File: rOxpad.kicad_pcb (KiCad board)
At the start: 2 copper layers, 68.3 x 65.1 mm, 25 parts, among them SW1 SW_Push, U1 ATmega16U2-A, U2 PRTR5V0U2X, Y1 16MHz

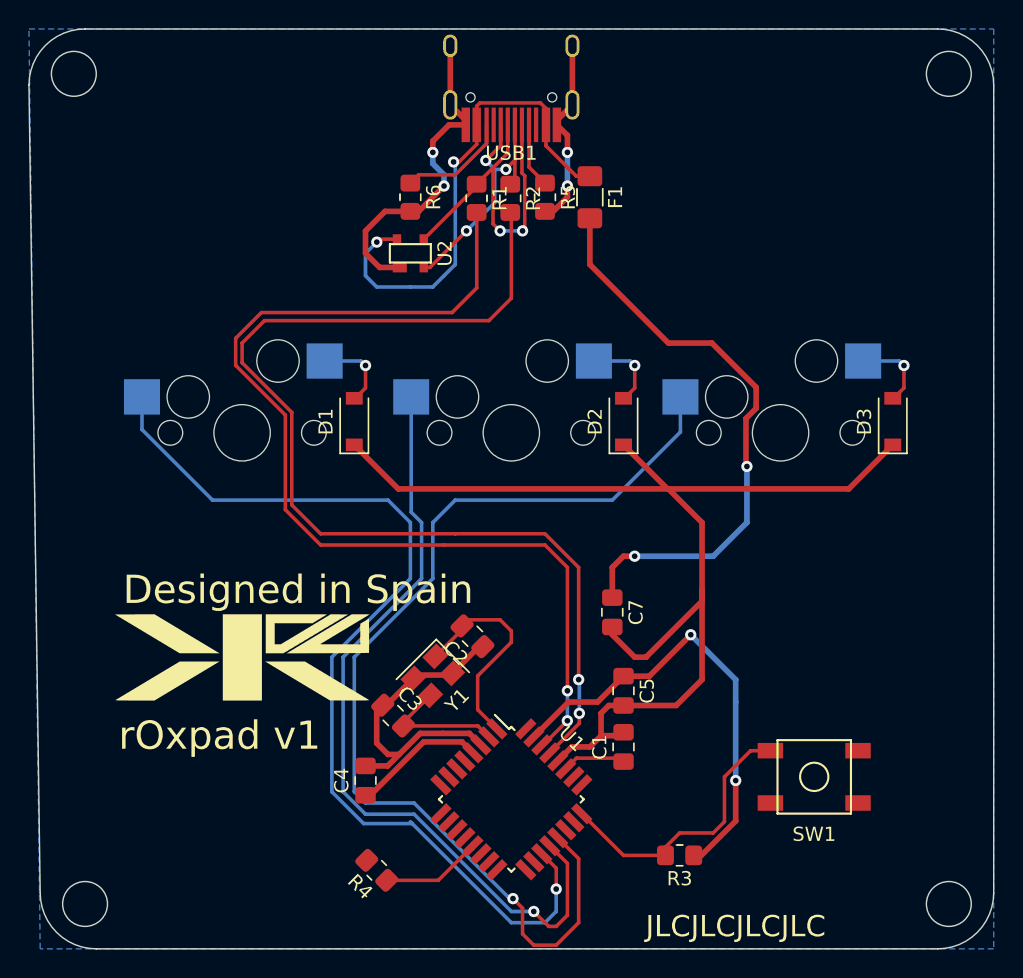
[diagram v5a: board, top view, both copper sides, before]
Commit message: it was a square oops
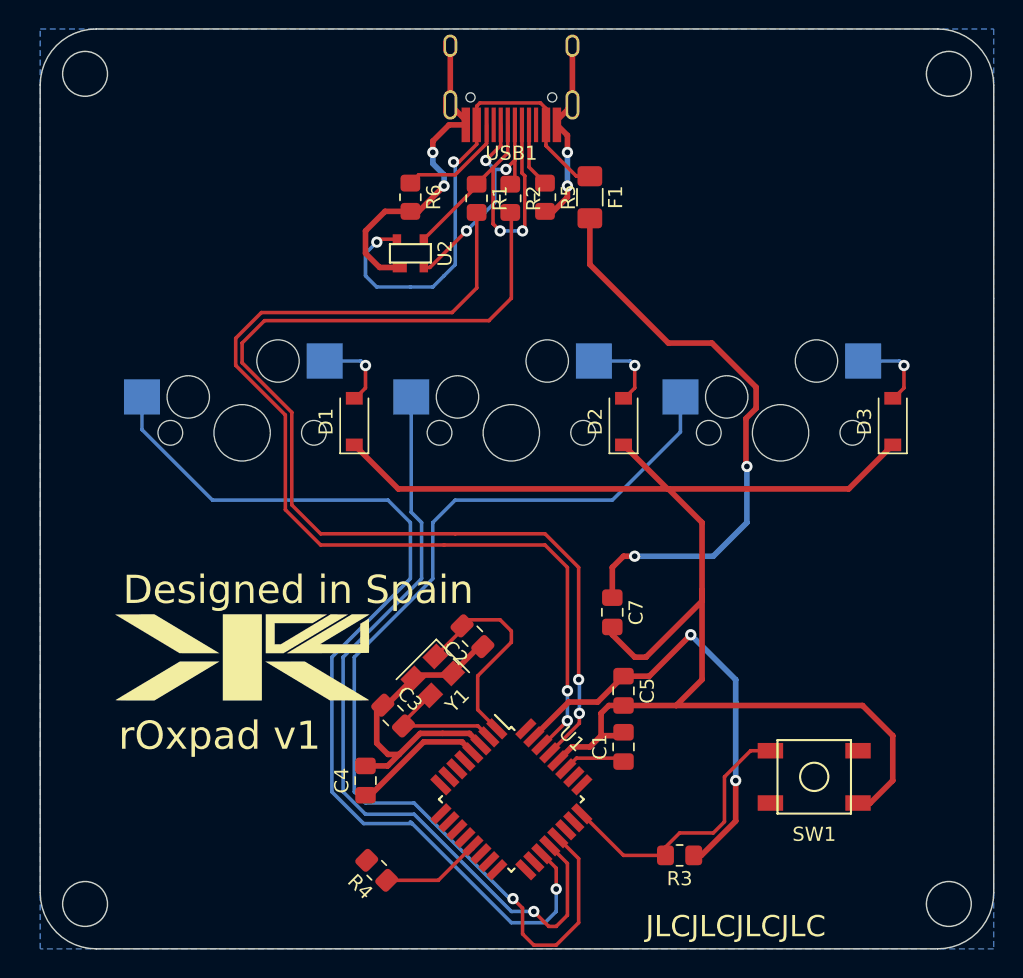
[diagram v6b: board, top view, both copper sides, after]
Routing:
- net GND: track 145.0 -> 167.5 mm
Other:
- board size 68.3 x 65.1 mm -> 67.5 x 65.1 mm
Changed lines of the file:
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@@
   (gr_line (start 77.7875 125.4125) (end 137.31875 125.4125) (layer "Edge.Cuts") (width 0.1))
   (gr_arc (start 137.31875 60.325) (mid 140.12508 61.48742) (end 141.2875 64.29375) (layer "Edge.Cuts") (width 0.1))
-  (gr_circle (center 76.2 63.5) (end 76.2 61.9125) (layer "Edge.Cuts") (width 0.1) (fill none))
-  (gr_line (start 137.31875 60.325) (end 76.99375 60.325) (layer "Edge.Cuts") (width 0.1))
+  (gr_circle (center 76.99375 63.5) (end 76.99375 61.9125) (layer "Edge.Cuts") (width 0.1) (fill none))
+  (gr_line (start 137.31875 60.325) (end 77.7875 60.325) (layer "Edge.Cuts") (width 0.1))
   (gr_line (start 141.2875 121.44375) (end 141.2875 79.375) (layer "Edge.Cuts") (width 0.1))
-  (gr_line (start 73.025 64.29375) (end 73.81875 121.44375) (layer "Edge.Cuts") (width 0.1))
+  (gr_line (start 73.81875 64.29375) (end 73.81875 121.44375) (layer "Edge.Cuts") (width 0.1))
   (gr_circle (center 76.99375 122.2375) (end 76.99375 120.65) (layer "Edge.Cuts") (width 0.1) (fill none))
   (gr_line (start 141.2875 79.375) (end 141.2875 64.29375) (layer "Edge.Cuts") (width 0.1))
-  (gr_arc (start 73.025 64.29375) (mid 74.18742 61.48742) (end 76.99375 60.325) (layer "Edge.Cuts") (width 0.1))
+  (gr_arc (start 73.81875 64.29375) (mid 74.98117 61.48742) (end 77.7875 60.325) (layer "Edge.Cuts") (width 0.1))
   (gr_text "Designed in Spain" (at 92.075 100.0125) (layer "F.SilkS")
     (effects (font (size 2 2) (thickness 0.15)))
@@
   (gr_text "JLCJLCJLCJLC" (at 123.03125 123.825) (layer "F.SilkS")
     (effects (font (size 1.5 1.5) (thickness 0.3)))
-  )
-  (dimension (type aligned) (layer "B.CrtYd")
-    (pts (xy 78.58125 79.375) (xy 73.025 79.375))
-    (height 0)
-    (gr_text "5.5563 mm" (at 75.803125 78.225) (layer "B.CrtYd")
-      (effects (font (size 1 1) (thickness 0.15)))
-    )
-    (format (units 3) (units_format 1) (precision 4))
-    (style (thickness 0.05) (arrow_length 1.27) (text_position_mode 0) (extension_height 0.58642) (extension_offset 0.5) keep_text_aligned)
-  )
-  (dimension (type aligned) (layer "B.CrtYd")
-    (pts (xy 135.73125 79.375) (xy 141.2875 79.375))
-    (height 0)
-    (gr_text "5.5563 mm" (at 138.509375 78.225) (layer "B.CrtYd")
-      (effects (font (size 1 1) (thickness 0.15)))
-    )
-    (format (units 3) (units_format 1) (precision 4))
-    (style (thickness 0.05) (arrow_length 1.27) (text_position_mode 0) (extension_height 0.58642) (extension_offset 0.5) keep_text_aligned)
   )
   (segment (start 103.657639 110.766953) (end 104.433889 111.543203) (width 0.4) (layer "F.Cu") (net 1))
@@
   (segment (start 114.05625 108.19375) (end 115.09375 108.19375) (width 0.4) (layer "F.Cu") (net 2))
   (segment (start 100.6 73.23125) (end 102.39375 71.4375) (width 0.4) (layer "F.Cu") (net 2))
+  (segment (start 132.55625 115.09375) (end 134.14375 113.50625) (width 0.4) (layer "F.Cu") (net 2))
   (segment (start 118.26875 92.86875) (end 131.03125 92.86875) (width 0.4) (layer "F.Cu") (net 2))
   (segment (start 96.8375 74.6125) (end 98.21875 73.23125) (width 0.4) (layer "F.Cu") (net 2))
@@
   (segment (start 97.63125 110.8625) (end 97.63125 108.601504) (width 0.4) (layer "F.Cu") (net 2))
   (segment (start 111.428186 111.125) (end 112.7125 111.125) (width 0.4) (layer "F.Cu") (net 2))
+  (segment (start 134.14375 113.50625) (end 134.14375 110.33125) (width 0.4) (layer "F.Cu") (net 2))
   (segment (start 105.139953 104.027293) (end 104.874788 104.027293) (width 0.4) (layer "F.Cu") (net 2))
   (segment (start 109.5375 73.23125) (end 110.125 73.23125) (width 0.4) (layer "F.Cu") (net 2))
@@
   (segment (start 102.8617 106.040381) (end 102.978858 105.923223) (width 0.4) (layer "F.Cu") (net 2))
   (segment (start 98.425 111.65625) (end 97.63125 110.8625) (width 0.4) (layer "F.Cu") (net 2))
+  (segment (start 134.14375 110.33125) (end 132.00625 108.19375) (width 0.4) (layer "F.Cu") (net 2))
   (segment (start 97.8375 77.2) (end 96.8375 76.2) (width 0.4) (layer "F.Cu") (net 2))
   (segment (start 111.125 67.85375) (end 110.38125 67.11) (width 0.4) (layer "F.Cu") (net 2))
@@
   (segment (start 120.65 100.80625) (end 120.65 100.0125) (width 0.4) (layer "F.Cu") (net 2))
   (segment (start 98.060047 108.172707) (end 98.325212 108.172707) (width 0.4) (layer "F.Cu") (net 2))
+  (segment (start 131.6875 115.09375) (end 132.55625 115.09375) (width 0.4) (layer "F.Cu") (net 2))
   (segment (start 103.93125 66.79) (end 102.83625 65.695) (width 0.4) (layer "F.Cu") (net 2))
   (segment (start 114.3 102.6375) (end 114.3 103.1875) (width 0.4) (layer "F.Cu") (net 2))
@@
   (segment (start 96.04375 89.75625) (end 99.15625 92.86875) (width 0.4) (layer "F.Cu") (net 2))
   (segment (start 96.8375 76.2) (end 96.8375 74.6125) (width 0.4) (layer "F.Cu") (net 2))
+  (segment (start 132.00625 108.19375) (end 118.81875 108.19375) (width 0.4) (layer "F.Cu") (net 2))
   (segment (start 104.999574 110.977518) (end 104.189009 110.166953) (width 0.4) (layer "F.Cu") (net 2))
   (segment (start 99.21875 111.65625) (end 98.425 111.65625) (width 0.4) (layer "F.Cu") (net 2))
@@
         (xy 141.2875 125.4125)
         (xy 73.81875 125.4125)
-        (xy 73.025 60.325)
+        (xy 73.81875 60.325)
         (xy 141.2875 60.325)
       )

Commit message: Fix sizing
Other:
- board size 67.5 x 65.1 mm -> 68.3 x 65.1 mm
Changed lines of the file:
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@@
   (gr_arc (start 141.2875 121.44375) (mid 140.12508 124.25008) (end 137.31875 125.4125) (layer "Edge.Cuts") (width 0.1))
   (gr_circle (center 138.1125 122.2375) (end 139.7 122.2375) (layer "Edge.Cuts") (width 0.1) (fill none))
-  (gr_arc (start 77.7875 125.4125) (mid 74.98117 124.25008) (end 73.81875 121.44375) (layer "Edge.Cuts") (width 0.1))
-  (gr_line (start 77.7875 125.4125) (end 137.31875 125.4125) (layer "Edge.Cuts") (width 0.1))
+  (gr_arc (start 76.99375 125.4125) (mid 74.187402 124.250083) (end 73.025 121.44375) (layer "Edge.Cuts") (width 0.1))
+  (gr_line (start 76.99375 125.4125) (end 137.31875 125.4125) (layer "Edge.Cuts") (width 0.1))
   (gr_arc (start 137.31875 60.325) (mid 140.12508 61.48742) (end 141.2875 64.29375) (layer "Edge.Cuts") (width 0.1))
-  (gr_circle (center 76.99375 63.5) (end 76.99375 61.9125) (layer "Edge.Cuts") (width 0.1) (fill none))
-  (gr_line (start 137.31875 60.325) (end 77.7875 60.325) (layer "Edge.Cuts") (width 0.1))
+  (gr_circle (center 76.2 63.5) (end 76.2 61.9125) (layer "Edge.Cuts") (width 0.1) (fill none))
+  (gr_line (start 137.31875 60.325) (end 76.99375 60.325) (layer "Edge.Cuts") (width 0.1))
   (gr_line (start 141.2875 121.44375) (end 141.2875 79.375) (layer "Edge.Cuts") (width 0.1))
-  (gr_line (start 73.81875 64.29375) (end 73.81875 121.44375) (layer "Edge.Cuts") (width 0.1))
-  (gr_circle (center 76.99375 122.2375) (end 76.99375 120.65) (layer "Edge.Cuts") (width 0.1) (fill none))
+  (gr_line (start 73.025 64.29375) (end 73.025 121.44375) (layer "Edge.Cuts") (width 0.1))
+  (gr_circle (center 76.2 122.2375) (end 76.2 120.65) (layer "Edge.Cuts") (width 0.1) (fill none))
   (gr_line (start 141.2875 79.375) (end 141.2875 64.29375) (layer "Edge.Cuts") (width 0.1))
-  (gr_arc (start 73.81875 64.29375) (mid 74.98117 61.48742) (end 77.7875 60.325) (layer "Edge.Cuts") (width 0.1))
+  (gr_arc (start 73.025 64.29375) (mid 74.18742 61.48742) (end 76.99375 60.325) (layer "Edge.Cuts") (width 0.1))
   (gr_text "Designed in Spain" (at 92.075 100.0125) (layer "F.SilkS")
     (effects (font (size 2 2) (thickness 0.15)))
@@
     (polygon
       (pts
-        (xy 141.2875 125.4125)
-        (xy 73.81875 125.4125)
-        (xy 73.81875 60.325)
-        (xy 141.2875 60.325)
+        (xy 140.49375 125.4125)
+        (xy 73.025 125.4125)
+        (xy 73.025 60.325)
+        (xy 140.49375 60.325)
       )
     )

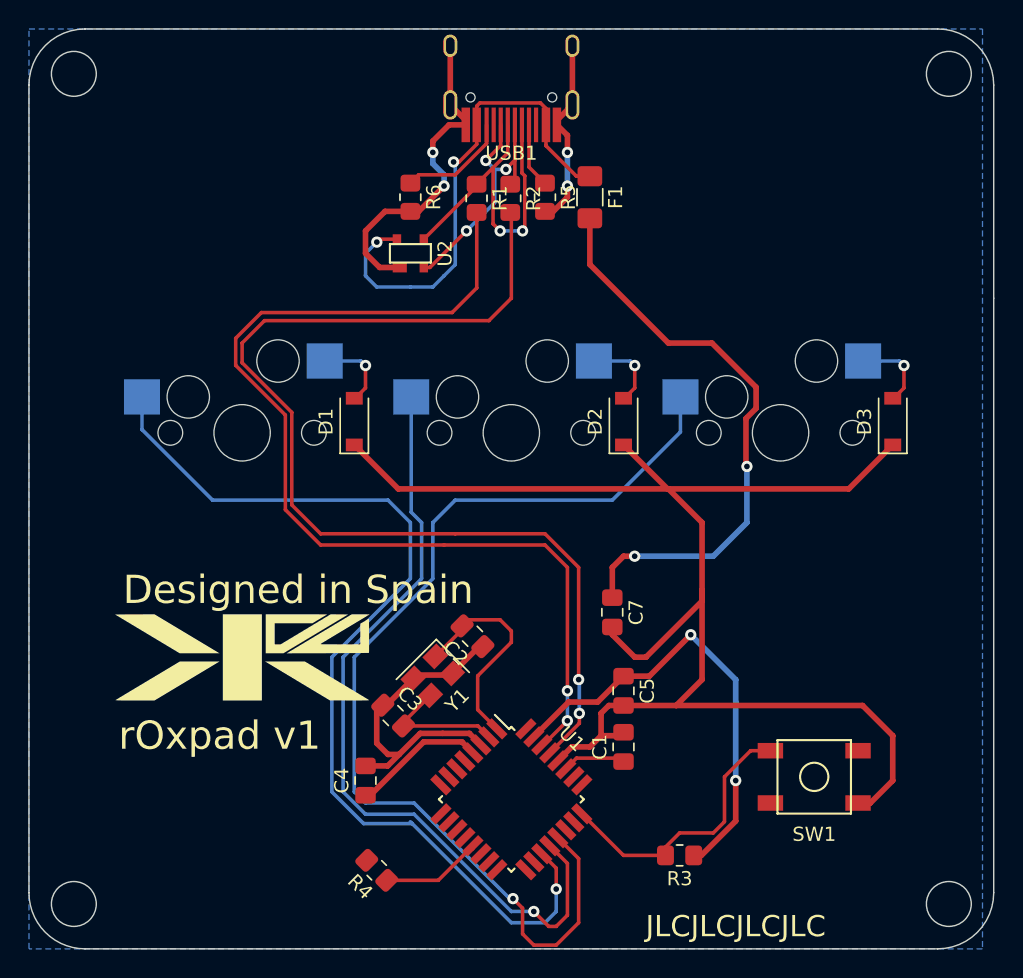
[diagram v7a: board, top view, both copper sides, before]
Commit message: Changed switch footprint (still same connections)
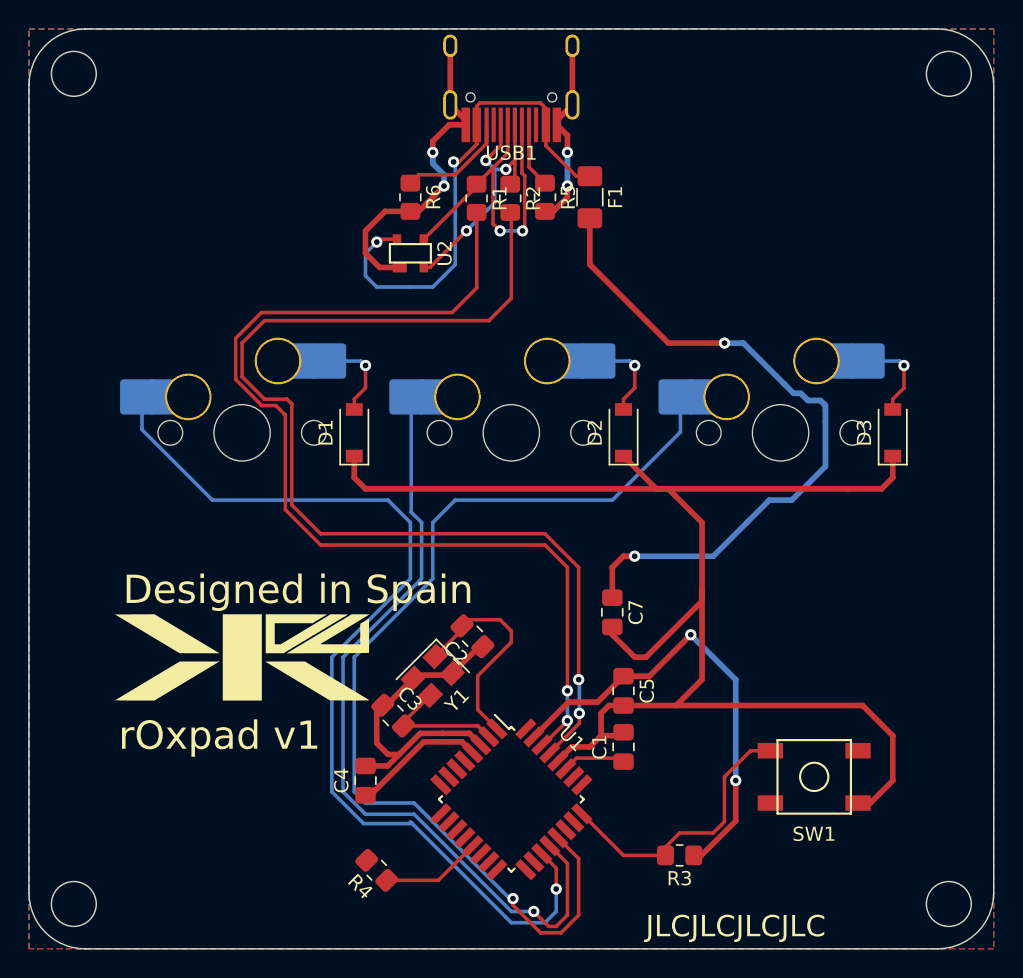
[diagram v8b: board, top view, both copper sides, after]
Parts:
- MX1, MX2, MX3: footprint MX_Only:MXOnly-1U-Hotswap -> marbastlib-mx:SW_MX_HS_1u; moved to B.Cu
- moved D1 0.79 mm to (96.0, 88.9)
- moved D2 0.79 mm to (115.1, 88.9)
- moved D3 0.79 mm to (134.1, 88.9)
- turned MX1 to 180 degrees
- turned MX2 to 180 degrees
- turned MX3 to 180 degrees
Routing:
- net +5V: track 83.6 -> 90.5 mm
- net KEY-2: track 72.7 -> 70.9 mm
- net Net-(R2-Pad2): track 75.5 -> 76.4 mm
- net GND: track 167.5 -> 168.4 mm
- net Net-(D3-Pad2): track 5.70 -> 6.46 mm
- net Net-(D2-Pad2): track 5.70 -> 6.46 mm
- net Net-(D1-Pad2): track 5.70 -> 6.46 mm
- net Net-(R1-Pad2): track 72.5 -> 73.1 mm
- added copper zone on F.Cu, net GND
